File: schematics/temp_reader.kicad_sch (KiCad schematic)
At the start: 11 parts, among them Q1 2N3904, Q2 2N3904, Q3 2N3904, U1 7-seg, U2 7-seg, U3 7-seg, U4 AM2320, U5 MG90S_servo

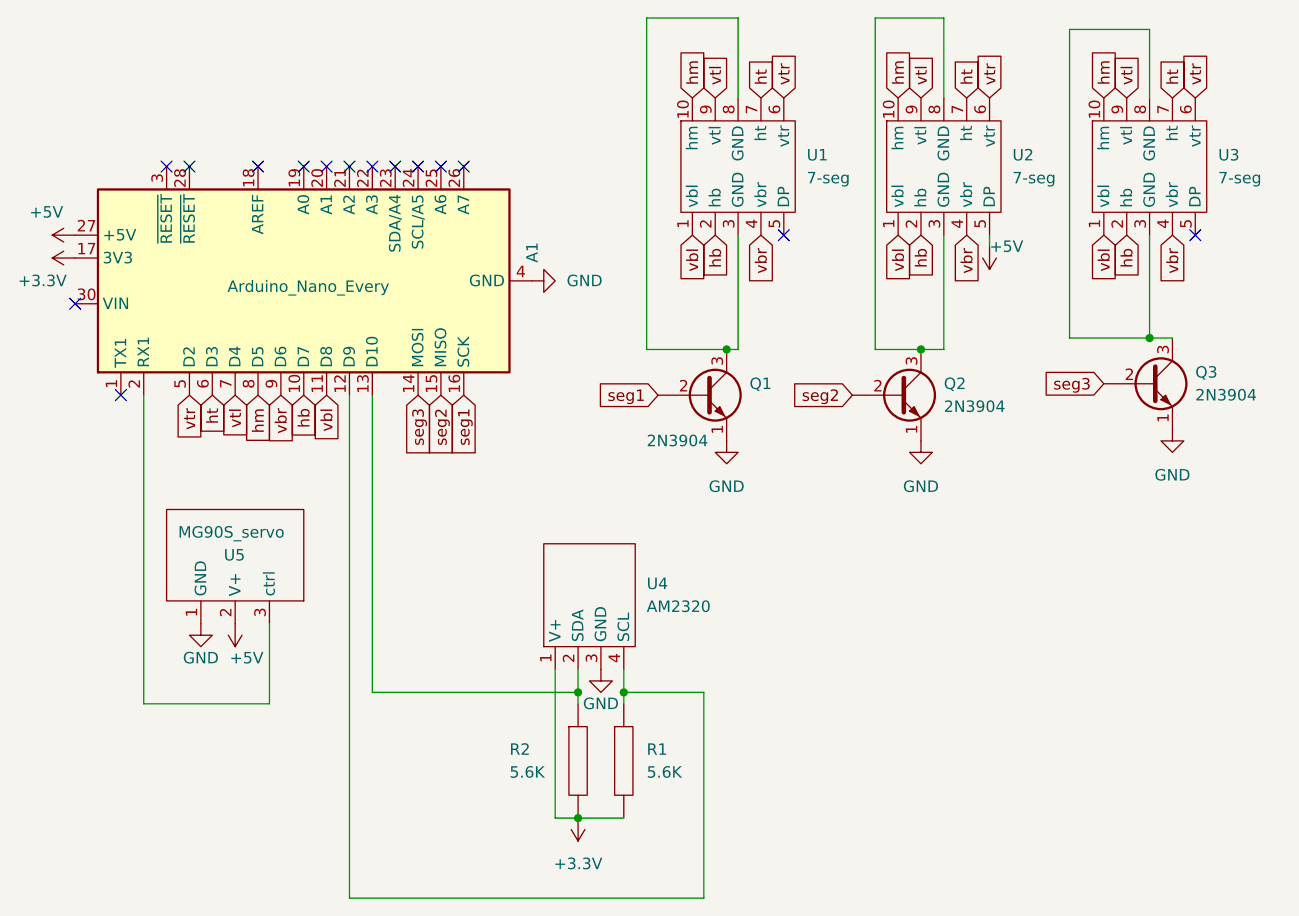
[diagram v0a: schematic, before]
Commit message: added tempurature module
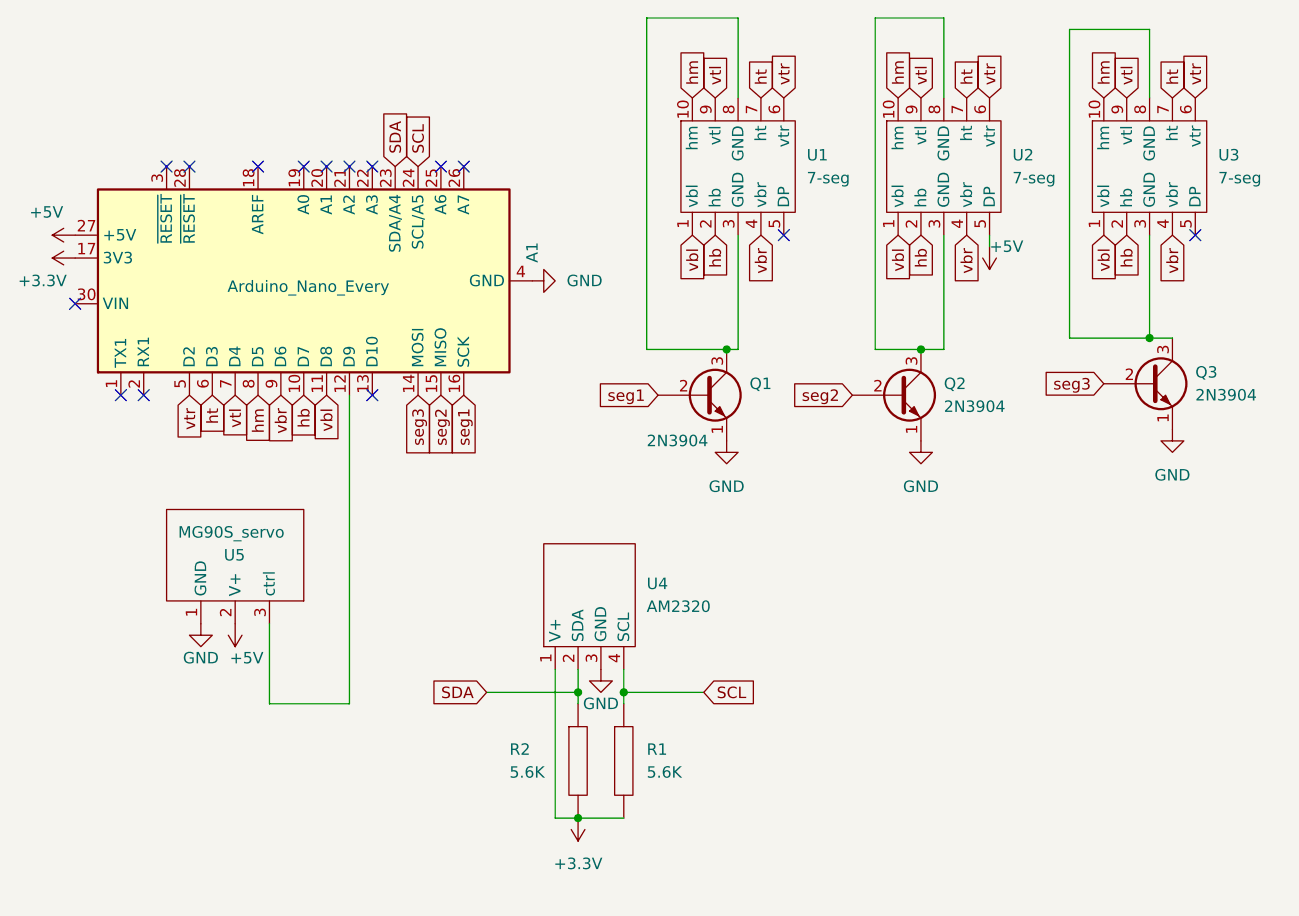
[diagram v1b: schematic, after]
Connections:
- net SCL: now reaches R1.1, U4.4 (SCL)
- net SCL: now also A1.24 (SCL/A5); no longer A1.12 (D9)
- net at U5.3 (ctrl): now also A1.12 (D9); no longer A1.2 (RX1)
- net SDA: now reaches R2.1, U4.2 (SDA)
- net SDA: now also A1.23 (SDA/A4); no longer A1.13 (D10)
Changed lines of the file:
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@@
 (kicad_sch (version 20230121) (generator eeschema)
   (paper "A4")
+  (junction (at 92.71 120.65) (diameter 0) (color 0 0 0 0)
+  )
   (junction (at 92.71 106.68) (diameter 0) (color 0 0 0 0)
-  )
-  (junction (at 92.71 120.65) (diameter 0) (color 0 0 0 0)
   )
   (junction (at 130.81 68.58) (diameter 0) (color 0 0 0 0)
@@
   (no_connect (at 62.23 48.26))
   (no_connect (at 80.01 48.26))
-  (no_connect (at 74.93 48.26))
-  (no_connect (at 72.39 48.26))
+  (no_connect (at 44.45 73.66))
   (no_connect (at 64.77 48.26))
   (no_connect (at 41.91 73.66))
@@
   (no_connect (at 49.53 48.26))
   (no_connect (at 115.57 55.88))
+  (no_connect (at 69.85 73.66))
   (no_connect (at 77.47 48.26))
-  (wire (pts (xy 69.85 106.68) (xy 92.71 106.68))
+  (wire (pts (xy 82.55 106.68) (xy 92.71 106.68))
     (stroke (width 0) (type default))
   )
@@
     (stroke (width 0) (type default))
   )
+  (wire (pts (xy 58.42 99.06) (xy 58.42 107.95))
+    (stroke (width 0) (type default))
+  )
+  (wire (pts (xy 58.42 107.95) (xy 67.31 107.95))
+    (stroke (width 0) (type default))
+  )
   (wire (pts (xy 92.71 104.14) (xy 92.71 106.68))
     (stroke (width 0) (type default))
   )
-  (wire (pts (xy 58.42 99.06) (xy 58.42 107.95))
+  (wire (pts (xy 125.73 31.75) (xy 133.35 31.75))
+    (stroke (width 0) (type default))
+  )
+  (wire (pts (xy 97.79 104.14) (xy 97.79 106.68))
+    (stroke (width 0) (type default))
+  )
+  (wire (pts (xy 100.33 68.58) (xy 109.22 68.58))
+    (stroke (width 0) (type default))
+  )
+  (wire (pts (xy 138.43 55.88) (xy 138.43 57.15))
+    (stroke (width 0) (type default))
+  )
+  (wire (pts (xy 110.49 55.88) (xy 110.49 68.58))
+    (stroke (width 0) (type default))
+  )
+  (wire (pts (xy 156.21 55.88) (xy 156.21 67.31))
+    (stroke (width 0) (type default))
+  )
+  (wire (pts (xy 133.35 55.88) (xy 133.35 68.58))
+    (stroke (width 0) (type default))
+  )
+  (wire (pts (xy 130.81 68.58) (xy 125.73 68.58))
+    (stroke (width 0) (type default))
+  )
+  (wire (pts (xy 109.22 68.58) (xy 110.49 68.58))
+    (stroke (width 0) (type default))
+  )
+  (wire (pts (xy 90.17 120.65) (xy 92.71 120.65))
+    (stroke (width 0) (type default))
+  )
+  (wire (pts (xy 156.21 40.64) (xy 156.21 33.02))
+    (stroke (width 0) (type default))
+  )
+  (wire (pts (xy 97.79 106.68) (xy 106.68 106.68))
+    (stroke (width 0) (type default))
+  )
+  (wire (pts (xy 110.49 31.75) (xy 100.33 31.75))
+    (stroke (width 0) (type default))
+  )
+  (wire (pts (xy 156.21 67.31) (xy 158.75 67.31))
+    (stroke (width 0) (type default))
+  )
+  (wire (pts (xy 97.79 106.68) (xy 97.79 107.95))
+    (stroke (width 0) (type default))
+  )
+  (wire (pts (xy 133.35 31.75) (xy 133.35 40.64))
+    (stroke (width 0) (type default))
+  )
+  (wire (pts (xy 147.32 67.31) (xy 156.21 67.31))
+    (stroke (width 0) (type default))
+  )
+  (wire (pts (xy 147.32 33.02) (xy 147.32 67.31))
+    (stroke (width 0) (type default))
+  )
+  (wire (pts (xy 125.73 68.58) (xy 125.73 31.75))
+    (stroke (width 0) (type default))
+  )
+  (wire (pts (xy 130.81 68.58) (xy 133.35 68.58))
+    (stroke (width 0) (type default))
+  )
+  (wire (pts (xy 100.33 31.75) (xy 100.33 68.58))
+    (stroke (width 0) (type default))
+  )
+  (wire (pts (xy 110.49 40.64) (xy 110.49 31.75))
+    (stroke (width 0) (type default))
+  )
+  (wire (pts (xy 67.31 107.95) (xy 67.31 73.66))
     (stroke (width 0) (type default))
   )
@@
     (stroke (width 0) (type default))
   )
-  (wire (pts (xy 125.73 31.75) (xy 133.35 31.75))
-    (stroke (width 0) (type default))
-  )
-  (wire (pts (xy 97.79 104.14) (xy 97.79 106.68))
-    (stroke (width 0) (type default))
-  )
-  (wire (pts (xy 100.33 68.58) (xy 109.22 68.58))
-    (stroke (width 0) (type default))
-  )
-  (wire (pts (xy 138.43 55.88) (xy 138.43 57.15))
-    (stroke (width 0) (type default))
-  )
-  (wire (pts (xy 110.49 55.88) (xy 110.49 68.58))
-    (stroke (width 0) (type default))
-  )
-  (wire (pts (xy 156.21 55.88) (xy 156.21 67.31))
-    (stroke (width 0) (type default))
-  )
-  (wire (pts (xy 133.35 55.88) (xy 133.35 68.58))
-    (stroke (width 0) (type default))
-  )
-  (wire (pts (xy 130.81 68.58) (xy 125.73 68.58))
-    (stroke (width 0) (type default))
-  )
-  (wire (pts (xy 67.31 73.66) (xy 67.31 129.54))
-    (stroke (width 0) (type default))
-  )
-  (wire (pts (xy 109.22 68.58) (xy 110.49 68.58))
-    (stroke (width 0) (type default))
-  )
-  (wire (pts (xy 90.17 120.65) (xy 92.71 120.65))
-    (stroke (width 0) (type default))
-  )
-  (wire (pts (xy 156.21 40.64) (xy 156.21 33.02))
-    (stroke (width 0) (type default))
-  )
-  (wire (pts (xy 97.79 106.68) (xy 106.68 106.68))
-    (stroke (width 0) (type default))
-  )
-  (wire (pts (xy 58.42 107.95) (xy 44.45 107.95))
-    (stroke (width 0) (type default))
-  )
-  (wire (pts (xy 110.49 31.75) (xy 100.33 31.75))
-    (stroke (width 0) (type default))
-  )
-  (wire (pts (xy 106.68 129.54) (xy 106.68 106.68))
-    (stroke (width 0) (type default))
-  )
-  (wire (pts (xy 156.21 67.31) (xy 158.75 67.31))
-    (stroke (width 0) (type default))
-  )
-  (wire (pts (xy 69.85 73.66) (xy 69.85 106.68))
-    (stroke (width 0) (type default))
-  )
-  (wire (pts (xy 67.31 129.54) (xy 106.68 129.54))
-    (stroke (width 0) (type default))
-  )
-  (wire (pts (xy 44.45 73.66) (xy 44.45 107.95))
-    (stroke (width 0) (type default))
-  )
-  (wire (pts (xy 97.79 106.68) (xy 97.79 107.95))
-    (stroke (width 0) (type default))
-  )
-  (wire (pts (xy 133.35 31.75) (xy 133.35 40.64))
-    (stroke (width 0) (type default))
-  )
-  (wire (pts (xy 147.32 67.31) (xy 156.21 67.31))
-    (stroke (width 0) (type default))
-  )
-  (wire (pts (xy 147.32 33.02) (xy 147.32 67.31))
-    (stroke (width 0) (type default))
-  )
-  (wire (pts (xy 125.73 68.58) (xy 125.73 31.75))
-    (stroke (width 0) (type default))
-  )
-  (wire (pts (xy 130.81 68.58) (xy 133.35 68.58))
-    (stroke (width 0) (type default))
-  )
-  (wire (pts (xy 100.33 31.75) (xy 100.33 68.58))
-    (stroke (width 0) (type default))
-  )
-  (wire (pts (xy 110.49 40.64) (xy 110.49 31.75))
-    (stroke (width 0) (type default))
+  (global_label "SDA" (shape input) (at 72.39 48.26 90) (fields_autoplaced)
+    (effects (font (size 1.27 1.27)) (justify left))
+    (property "Intersheetrefs" "${INTERSHEET_REFS}" (at 72.39 41.7861 90)
+      (effects (font (size 1.27 1.27)) (justify left) hide)
+    )
   )
   (global_label "seg2" (shape input) (at 123.19 73.66 180) (fields_autoplaced)
@@
     )
   )
+  (global_label "SCL" (shape input) (at 74.93 48.26 90) (fields_autoplaced)
+    (effects (font (size 1.27 1.27)) (justify left))
+    (property "Intersheetrefs" "${INTERSHEET_REFS}" (at 74.93 41.8466 90)
+      (effects (font (size 1.27 1.27)) (justify left) hide)
+    )
+  )
   (global_label "hm" (shape input) (at 128.27 40.64 90) (fields_autoplaced)
     (effects (font (size 1.27 1.27)) (justify left))
@@
     )
   )
+  (global_label "SDA" (shape input) (at 82.55 106.68 180) (fields_autoplaced)
+    (effects (font (size 1.27 1.27)) (justify right))
+    (property "Intersheetrefs" "${INTERSHEET_REFS}" (at 76.0761 106.68 0)
+      (effects (font (size 1.27 1.27)) (justify right) hide)
+    )
+  )
   (global_label "vbl" (shape input) (at 64.77 73.66 270) (fields_autoplaced)
     (effects (font (size 1.27 1.27)) (justify right))
@@
       (effects (font (size 1.27 1.27)) (justify left) hide)
     )
+  )
+  (global_label "SCL" (shape input) (at 106.68 106.68 0) (fields_autoplaced)
+    (effects (font (size 1.27 1.27)) (justify left))
+    (property "Intersheetrefs" "${INTERSHEET_REFS}" (at 113.0934 106.68 0)
+      (effects (font (size 1.27 1.27)) (justify left) hide)
+    )

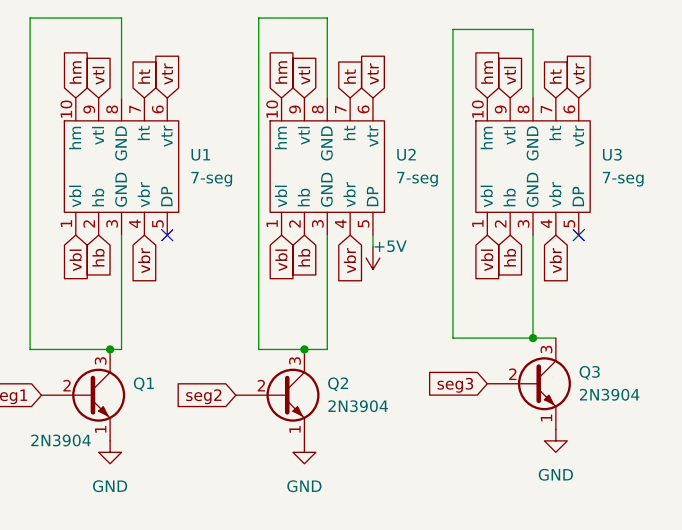
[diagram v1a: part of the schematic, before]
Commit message: using 3.3v for decimal LED
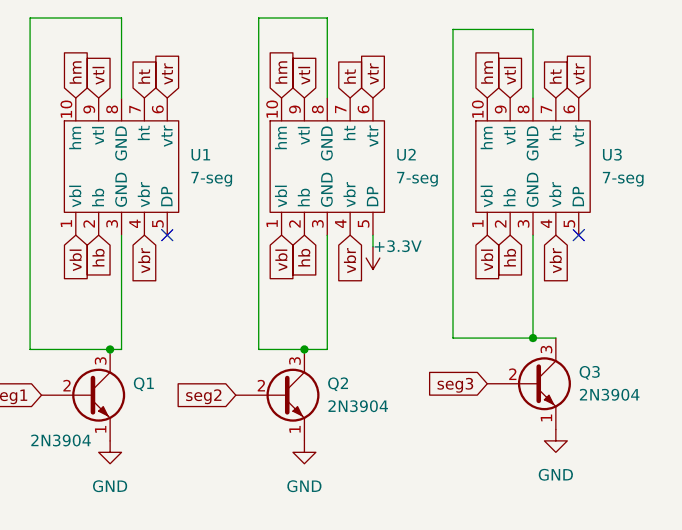
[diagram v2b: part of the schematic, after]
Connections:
- net +3.3V: now also U2.5 (DP)
- net +5V: no longer U2.5 (DP)
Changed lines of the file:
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@@
+    )
+  )
+  (symbol (lib_id "power:+3.3V") (at 138.43 57.15 180) (unit 1)
+    (in_bom yes) (on_board yes) (dnp no)
+    (property "Reference" "#PWR01" (at 138.43 53.34 0)
+      (effects (font (size 1.27 1.27)) hide)
+    )
+    (property "Value" "+3.3V" (at 138.43 57.15 0)
+      (effects (font (size 1.27 1.27)) (justify right))
+    )
+    (property "Footprint" "" (at 138.43 57.15 0)
+      (effects (font (size 1.27 1.27)) hide)
+    )
+    (property "Datasheet" "" (at 138.43 57.15 0)
+      (effects (font (size 1.27 1.27)) hide)
+    )
+    (pin "1")
+    (instances
+      (project "temp_reader"
+        (path "/fa83d0dc-8fb2-450b-af06-da96bef65c78"
+          (reference "#PWR01") (unit 1)
+        )
+      )
     )
   )
@@
         )
       )
-    )
-  )
-  (symbol (lib_id "power:+5V") (at 138.43 57.15 180) (unit 1)
-    (in_bom yes) (on_board yes) (dnp no)
-    (property "Reference" "#PWR01" (at 138.43 53.34 0)
-      (effects (font (size 1.27 1.27)) hide)
-    )
-    (property "Value" "+5V" (at 138.43 57.15 0)
-      (effects (font (size 1.27 1.27)) (justify right))
-    )
-    (property "Footprint" "" (at 138.43 57.15 0)
-      (effects (font (size 1.27 1.27)) hide)
-    )
-    (property "Datasheet" "" (at 138.43 57.15 0)
-      (effects (font (size 1.27 1.27)) hide)
-    )
-    (pin "1")
-    (instances
-      (project "temp_reader"
-        (path "/fa83d0dc-8fb2-450b-af06-da96bef65c78"
-          (reference "#PWR01") (unit 1)
-        )
-      )

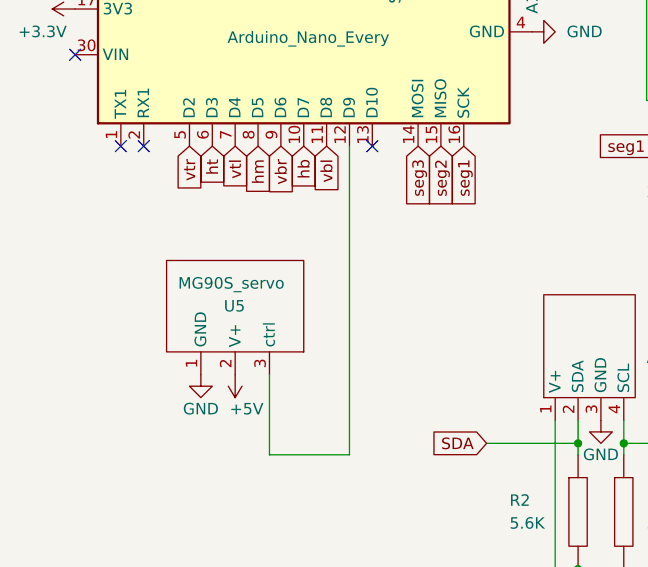
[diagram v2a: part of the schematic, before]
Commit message: updated servo model and adjusted temp sensor blueprint
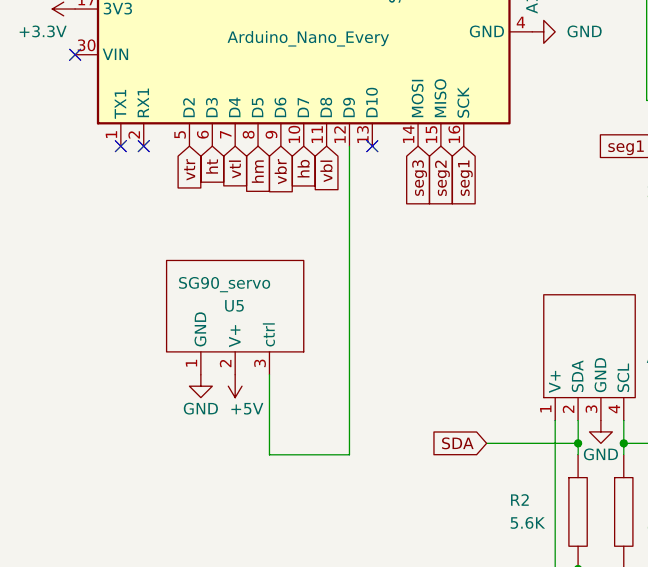
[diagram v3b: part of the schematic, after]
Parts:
- U5: value MG90S_servo -> SG90_servo
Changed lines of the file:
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@@
       (effects (font (size 1.27 1.27)) (justify left))
     )
-    (property "Value" "MG90S_servo" (at 48.26 88.9 0)
+    (property "Value" "SG90_servo" (at 48.26 88.9 0)
       (effects (font (size 1.27 1.27)) (justify left))
     )
